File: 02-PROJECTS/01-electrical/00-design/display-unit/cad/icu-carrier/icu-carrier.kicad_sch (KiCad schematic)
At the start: 115 parts, among them J1 DT13-06PA, J2 backlight out, J3 DT13-12PA, J4 ME817EV CN8 - 2x8 host header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, J5 Teensy 4.1 socket - 2 x 24 fe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, Q1 SQD50P06 class, >= 60 V, Q2 MMBT3904, Q3 DMG3415U class P-FET, SOT-23 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, Q4 MMBT3904, SW1 IC22, U1 LMR36015FSCQ-Q1, U2 VN5E class, >= 6 A - DNP, U3 TCAN1042HVDRQ1, U4 LM393, U5 74LVC1G17, U7 Adafruit 4517 LSM6DSOX+LIS3MD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, U8 XIAO ESP32C3 2x7 socket (Seee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

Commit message: Electrical: the carriers corrected before the order - six TVS diodes drawn backwards, the wake switch's pins swapped, an unconnected zener, the bulk capacitor's value (D-547)
Y42 done; Y44 (an independent read of the boards, and the gate drive of two P-FETs) holds the board order Y18. DU and CU carrier fab zips rebuilt; the earlier ones must not be ordered. The board check now holds transistors and diodes to their makers' pin-outs.

Co-Authored-By: Claude Opus 5.5 <noreply@anthropic.com>
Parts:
- C1: value 100u 63V -> 68u 63V
- D20: symbol icu-carrier:D_Zener -> icu-carrier:D_Zener_SOT23
- D24, D26: symbol icu-carrier:D_TVS -> icu-carrier:D_TVS_Uni
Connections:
- net +12V_BL: now also D26.1 (K); no longer D26.2 (A2)
- net +12V_LOGIC: now also D24.1 (K); no longer D24.2 (A2)
- net GND: now also D24.2 (A), D26.2 (A); no longer D24.1 (A1), D26.1 (A1)
- net at D20.2 (NC), D21.3 (COM), R30.1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: now also D20.3 (K)
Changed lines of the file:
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@@
 	(title_block
 		(title "ICU carrier - H-001")
-		(rev "0.03")
+		(rev "0.04")
 		(company "RX-7 FB electrical build")
 		(comment 1 "Drawn by hand. The record is 02-PROJECTS/01-electrical/data/icu_channels.csv - where this sheet and a row disagree, the row is right.")
@@
 			)
 		)
-		(property "Value" "100u 63V"
+		(property "Value" "68u 63V"
 			(at 92.1 42.04 0)
 			(show_name no)
@@
 	)
 	(symbol
-		(lib_id "icu-carrier:D_Zener")
+		(lib_id "icu-carrier:D_Zener_SOT23")
 		(at 71.12 427.99 90)
 		(unit 1)
@@
 		)
 		(pin "2"
-		)
+		) (pin "3")
 		(instances
 			(project "icu-carrier"
@@
 	)
 	(symbol
-		(lib_id "icu-carrier:D_TVS")
+		(lib_id "icu-carrier:D_TVS_Uni")
 		(at 73.66 40.64 90)
 		(unit 1)
@@
 	)
 	(symbol
-		(lib_id "icu-carrier:D_TVS")
+		(lib_id "icu-carrier:D_TVS_Uni")
 		(at 73.66 114.3 90)
 		(unit 1)

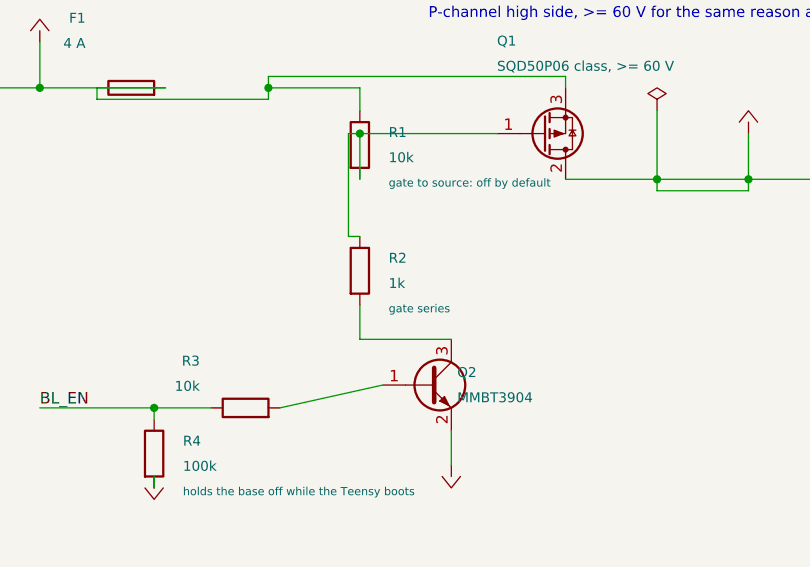
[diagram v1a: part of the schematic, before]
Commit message: Electrical: the two P-FETs' gate drive brought down, the order text names the parts as they are (D-547)
CU Q3: R43 18 k, inside its gate limit at the 53 V clamp. DU Q1: R2 10 k, inside to 40 V on the rail; a gate zener for the clamp case is held for one fix pass with the independent review's findings (Y44). No fab file changed; the cart file follows. Y18's steps rebuilt.

Co-Authored-By: Claude Opus 5.5 <noreply@anthropic.com>
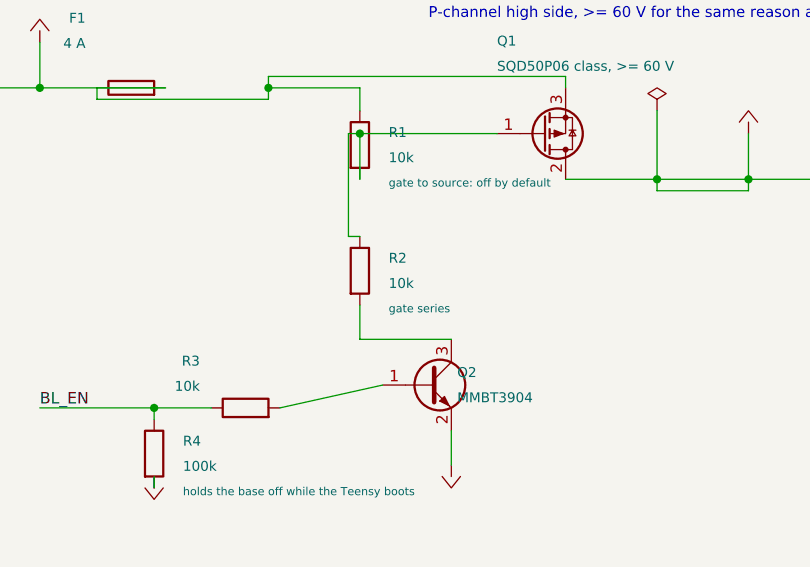
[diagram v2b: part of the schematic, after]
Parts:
- R2: value 1k -> 10k
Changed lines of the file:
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@@
 	(title_block
 		(title "ICU carrier - H-001")
-		(rev "0.04")
+		(rev "0.05")
 		(company "RX-7 FB electrical build")
 		(comment 1 "Drawn by hand. The record is 02-PROJECTS/01-electrical/data/icu_channels.csv - where this sheet and a row disagree, the row is right.")
@@
 			)
 		)
-		(property "Value" "1k"
+		(property "Value" "10k"
 			(at 122.58 128.4 0)
 			(show_name no)

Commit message: Electrical: the independent read's findings fixed on the boards before the order, and the Display Unit's brake-warning input given its pull-up (D-549)
Y44 done; Y18 (the board order) opens. DU carrier rev 0.06: road-speed input IC08 re-laid, a 15 V gate zener and 4.7 k on the backlight switch, four vias at each backlight layer change, brake warning IC06 pulled up to 3V3 (found while the changes were read back - it could never have read high), tell-tale dividers 22 k, MMBT5551 and SL310A on the rails clamped at 53 V. CU carrier rev 0.07, values only: C27 100 nF, Q1 / Q2 SQ2364EES, Q4 MMBT5551, D1 SL310A. Panel: the encoders' lug slots to Bourns' layout. Two assembly drawings in each fab folder in place of silkscreen references.

ERC 0, DRC 0 / 0 / 0, check.py 0 mismatches on all five boards. The DU carrier's and the panel's fab zips are rebuilt under the same names; the CU carrier's and the upper board's are unchanged. Cart 98 lines. Record: icu_channels IC06 IC08 IC09 IC12 IC13, dcu_channels SN23 SN24, parts P106 P107 P147 P149 P169 P170 P203, Y18 / F3 / F5 briefs and steps. D-548's DT13 question is untouched (V-117).

Co-Authored-By: Claude Opus 5.5 <noreply@anthropic.com>
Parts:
- added D27: MM3Z15VT1G, Diode_SMD:D_SOD-323, symbol icu-carrier:D_TVS_Uni
- D23, D25: value SS34 -> SL310A
- Q2: value MMBT3904 -> MMBT5551
- R16: value 47k -> 1k
- R2: value 10k -> 4.7k
- R21, R23, R25: value 47k -> 22k
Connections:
- net +3V3: now also R17.2
- net GND: now also JP8B1.1; no longer R17.2, R37.2
- net ICU_B8: now also R36.1; no longer D22.3 (COM), JP8B1.1, R36.2, R37.1, U5.2
- net BL_GATE: now reaches Q1.1 (G), R1.2, R2.1
- net BL_GATE: now also D27.2 (A)
- net BL_FUSED: now reaches F1.1, Q1.3 (S), R1.1
- net BL_FUSED: now also D27.1 (K)
- net at JP8B1.2: now also R37.2; no longer R36.1
- new net IC08_IN: D22.3 (COM), R36.2, R37.1, U5.2
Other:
- note added: "R17 pulls the node UP to +3V3 (the arrow under it is the +3V3 rail). Both switches open: 3.3 V. Either closed: 0.30 V = warn (IC06)."
- note added: "R36 (10 k) is in series with the input. J8A pulls the input to +3V3 for an open-collector sensor. J8B grounds R37 to make a 10 k / 4.7 k divider for a push-pull 12 V output, which lands at 12 x 4.7/14.7 = 3.84 V - above the rail, which is exactly why the BAT54S is there and is not optional. Fit one jumper, never both. Pulses per mile is a config value, trued once against a measured mile (D-272)."
- note removed: "J8A pulls the node to +3V3 for an open-collector sensor. J8B makes a 10 k / 4.7 k divider for a push-pull output, which lands at 12 x 4.7/14.7 = 3.84 V - above the rail, which is exactly why the BAT54S is there and is not optional. Pulses per mile is a config value, trued once against a measured mile (D-272)."
- moved on the sheet: JP8B1, R36

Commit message: Electrical: the ICU carrier drawn with one DRC13-24PA, the tach alone on pin 6; the board 110 x 84 (D-590, D-591, D-592)
Y63 done. J1 and J3 become one Deutsch DRC13-24PA (footprint from TE's drawing, TE's model in the
library and on the board), the board grows 4 mm at the connector edge, re-routed under the project's
own rules: ERC 0, DRC 0 with parity, check.py icu 105 / 0. The cavity map is permuted so the tach
(TACH_HV, 2.5 mm) has no live neighbour (D-592); every row, step and the engine handover follow.
Fab package, BOM, assembly, STEP, the DU mock-up (34 / 34) and the bench enclosure rebuilt; the DRC
family in the connector builder (the receptacle from TE's model); the scene re-exported. The record
files also carry Y62 / Y50's rows and block 01.60 (the next commit's boards).

Co-Authored-By: Claude Opus 5.5 <noreply@anthropic.com>
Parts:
- added unit 3 of J1
- J1: value DT13-06PA -> DRC13-24PA; footprint icu-carrier:DT13-06PA -> icu-carrier:DRC13-24PA; symbol icu-carrier:Conn_01x06 -> icu-carrier:DRC13-24PA; Drop DP-ICU-A -> DP-ICU
- J1: renamed from J3; value DT13-12PA -> DRC13-24PA; footprint icu-carrier:DT13-12PA -> icu-carrier:DRC13-24PA; symbol icu-carrier:Conn_01x12 -> icu-carrier:DRC13-24PA; Drop DP-ICU-B -> DP-ICU
- U4: Note on the +5 V rail - see above -> LM393: unit A the tach comparator on the +5 V rail; unit B 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
- U4: Note the spare half - inputs tied together so it cannot oscillate -> LM393: unit A the tach comparator on the +5 V rail; unit B 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
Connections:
- net GND: now also J1.21 (Pin_21); no longer J1.3 (Pin_3)
- net ICU_B1: now also J1.7 (Pin_7); no longer J1.1 (Pin_1)
- net ICU_B10: now also J1.16 (Pin_16); no longer J1.10 (Pin_10)
- net ICU_B11: now also J1.17 (Pin_17); no longer J1.11 (Pin_11)
- net ICU_B12: now also J1.22 (Pin_22); no longer J1.12 (Pin_12)
- net ICU_B2: now also J1.8 (Pin_8); no longer J1.2 (Pin_2)
- net ICU_B3: now also J1.9 (Pin_9); no longer J1.3 (Pin_3)
- net ICU_B4: now also J1.6 (Pin_6); no longer J1.4 (Pin_4)
- net ICU_B5: now also J1.11 (Pin_11); no longer J1.5 (Pin_5)
- net ICU_B6: now also J1.10 (Pin_10); no longer J1.6 (Pin_6)
- net ICU_B7: now also J1.13 (Pin_13); no longer J1.7 (Pin_7)
- net ICU_B8: now also J1.14 (Pin_14); no longer J1.8 (Pin_8)
- net at D25.2 (A): now also J1.3 (Pin_3); no longer J1.6 (Pin_6)
- no-connect marks 27 -> 33
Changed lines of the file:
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@@
 	)
 	(symbol
+		(lib_id "icu-carrier:DRC13-24PA")
+		(at 190.5 50.8 0)
+		(unit 3)
+		(body_style 1)
+		(exclude_from_sim no)
+		(in_bom yes)
+		(on_board yes)
+		(in_pos_files yes)
+		(dnp no)
+		(property "Reference" "J1"
+			(at 182.88 34.16 0)
+			(show_name no)
+			(do_not_autoplace no)
+			(effects
+				(font
+					(size 1.1 1.1)
+				)
+				(justify left)
+			)
+		)
+		(property "Value" "DRC13-24PA"
+			(at 182.88 36.96 0)
+			(show_name no)
+			(do_not_autoplace no)
+			(effects
+				(font
+					(size 1.1 1.1)
+				)
+				(justify left)
+			)
+		)
+		(property "Footprint" "icu-carrier:DRC13-24PA"
+			(at 190.5 50.8 0)
+			(hide yes)
+			(show_name no)
+			(do_not_autoplace no)
+			(effects
+				(font
+					(size 1.27 1.27)
+				)
+			)
+		)
+		(property "Datasheet" ""
+			(at 190.5 50.8 0)
+			(show_name no)
+			(do_not_autoplace no)
+			(effects
+				(font
+					(size 1.27 1.27)
+				)
+			)
+		)
+		(property "Description" ""
+			(at 190.5 50.8 0)
+			(show_name no)
+			(do_not_autoplace no)
+			(effects
+				(font
+					(size 1.27 1.27)
+				)
+			)
+		)
+		(property "Drop" "DP-ICU"
+			(at 182.88 39.76 0)
+			(show_name no)
+			(do_not_autoplace no)
+			(effects
+				(font
+					(size 0.9 0.9)
+				)
+				(justify left)
+			)
+		)
+		(pin "19"
+		)
+		(pin "20"
+		)
+		(pin "23"
+		)
+		(pin "24"
+		)
+		(pin "18"
+		)
+		(pin "12"
+		)
+		(instances
+			(project "icu-carrier"
+				(path "/c75d3432-4fb5-46c2-a0c1-15c6416c4dd0"
+					(reference "J1")
+					(unit 3)
+				)
+			)
+		)
+	)
+	(no_connect
+		(at 185.42 45.72)
+	)
+	(no_connect
+		(at 185.42 48.26)
+	)
+	(no_connect
+		(at 185.42 50.8)
+	)
+	(no_connect
+		(at 185.42 53.34)
+	)
+	(no_connect
+		(at 185.42 55.88)
+	)
+	(no_connect
+		(at 185.42 58.42)
+	)
+	(symbol
 		(lib_id "icu-carrier:+5V")
 		(at 269.24 231.14 0)
@@
 			)
 		)
-		(property "Note" "on the +5 V rail - see above"
+		(property "Note" "LM393: unit A the tach comparator on the +5 V rail; unit B the spare half - inputs tied together so it cannot oscillate"
 			(at 121.92 438.54 0)
 			(show_name no)
@@
 	)
 	(symbol
-		(lib_id "icu-carrier:Conn_01x06")
+		(lib_id "icu-carrier:DRC13-24PA")
 		(at 38.1 68.58 0)
 		(mirror y)
@@
 			)
 		)
-		(property "Value" "DT13-06PA"
+		(property "Value" "DRC13-24PA"
 			(at 30.48 54.74 0)
 			(show_name no)
@@
 			)
 		)
-		(property "Footprint" "icu-carrier:DT13-06PA"
+		(property "Footprint" "icu-carrier:DRC13-24PA"
 			(at 38.1 68.58 0)
 			(hide yes)
@@
 			)
 		)
-		(property "Drop" "DP-ICU-A"
+		(property "Drop" "DP-ICU"
 			(at 30.48 57.54 0)
 			(show_name no)
@@
 		(pin "2"
 		)
-		(pin "3"
+		(pin "21"
 		)
 		(pin "4"
@@
 		(pin "5"
 		)
-		(pin "6"
+		(pin "3"
 		)
 		(instances
@@
 	)
 	(symbol
-		(lib_id "icu-carrier:Conn_01x12")
+		(lib_id "icu-carrier:DRC13-24PA")
 		(at 30.48 274.32 0)
 		(mirror y)
-		(unit 1)
+		(unit 2)
 		(body_style 1)
 		(exclude_from_sim no)
@@
 		(in_pos_files yes)
 		(dnp no)
-		(property "Reference" "J3"
+		(property "Reference" "J1"
 			(at 17.78 247.52 0)
 			(show_name no)
@@
 			)
 		)
-		(property "Value" "DT13-12PA"
+		(property "Value" "DRC13-24PA"
 			(at 17.78 250.32 0)
 			(show_name no)
@@
 			)
 		)
-		(property "Footprint" "icu-carrier:DT13-12PA"
+		(property "Footprint" "icu-carrier:DRC13-24PA"
 			(at 30.48 274.32 0)
 			(hide yes)
@@
 			)
 		)
-		(property "Drop" "DP-ICU-B"
+		(property "Drop" "DP-ICU"
 			(at 17.78 253.12 0)
 			(show_name no)
@@
 			)
 		)
-		(pin "1"
+		(pin "7"
 		)
-		(pin "10"
+		(pin "16"
 		)
-		(pin "11"
+		(pin "17"
 		)
-		(pin "12"
+		(pin "22"
 		)
-		(pin "2"
+		(pin "8"
 		)
-		(pin "3"
+		(pin "9"
 		)
-		(pin "4"
+		(pin "6"
 		)
-		(pin "5"
+		(pin "11"
 		)
-		(pin "6"
+		(pin "10"
 		)
-		(pin "7"
+		(pin "13"
 		)
-		(pin "8"
+		(pin "14"
 		)
-		(pin "9"
+		(pin "15"
 		)
 		(instances
 			(project "icu-carrier"
 				(path "/c75d3432-4fb5-46c2-a0c1-15c6416c4dd0"
-					(reference "J3")
-					(unit 1)
+					(reference "J1")
+					(unit 2)
 				)
 			)
@@
 			)
 		)
-		(property "Note" "the spare half - inputs tied together so it cannot oscillate"
+		(property "Note" "LM393: unit A the tach comparator on the +5 V rail; unit B the spare half - inputs tied together so it cannot oscillate"
 			(at 308 430.92 0)
 			(show_name no)
